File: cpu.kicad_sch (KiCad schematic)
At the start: 53 parts, among them IC12 DS2401+, IC13 ARM250, IC20 74HC138, IC27 74AC32, IC8 74HCT14, X100 40.0MHz, X4 72.0MHz, X5 25.175MHz

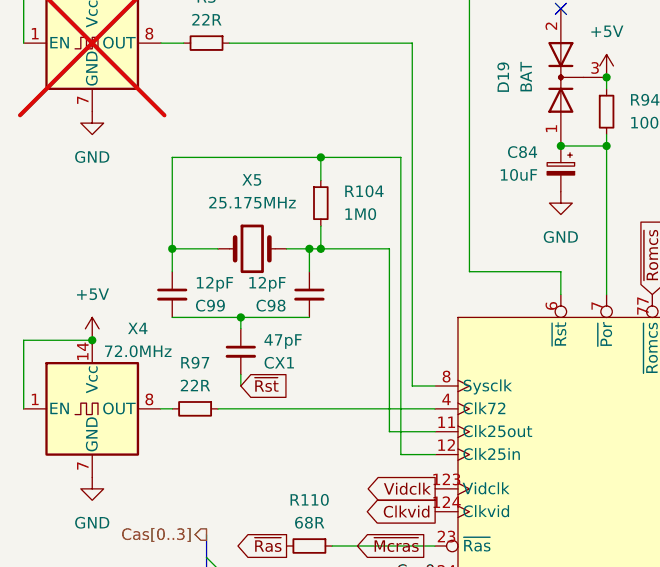
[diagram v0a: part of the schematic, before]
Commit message: fix CX1
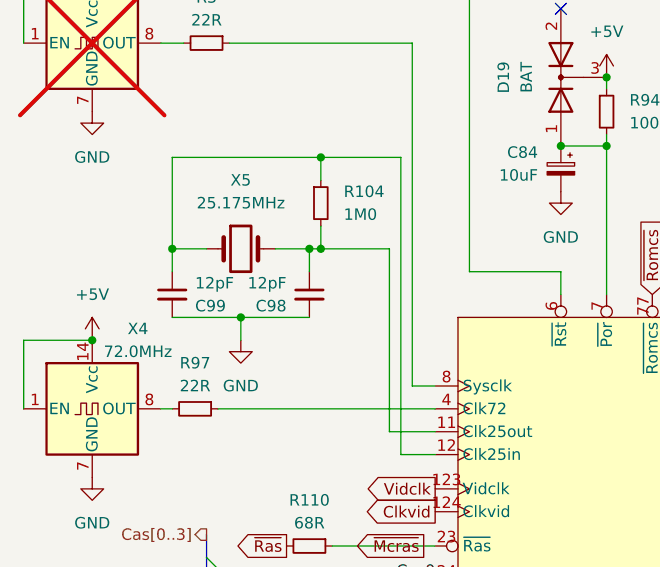
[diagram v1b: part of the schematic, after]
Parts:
- removed CX1: 47pF, Capacitor_THT:C_Axial_L5.1mm_D3.1mm_P12.50mm_Horizontal, symbol Device:C_Small
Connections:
- net GND: now also C98.2, C99.2
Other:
- moved on the sheet: X5
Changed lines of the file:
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@@
 	)
 	(junction
-		(at 71.12 88.9)
-		(diameter 0)
-		(color 0 0 0 0)
-	)
-	(junction
 		(at 187.96 86.36)
 		(diameter 0)
@@
 		(color 0 0 0 0)
 	)
+	(junction
+		(at 71.12 88.9)
+		(diameter 0)
+		(color 0 0 0 0)
+	)
 	(no_connect
 		(at 382.27 57.15)
@@
 	(wire
 		(pts
-			(xy 76.2 81.28) (xy 78.74 81.28)
+			(xy 74.93 81.28) (xy 78.74 81.28)
 		)
 		(stroke
@@
 	(wire
 		(pts
-			(xy 71.12 88.9) (xy 71.12 90.17)
-		)
-		(stroke
-			(width 0)
-			(type default)
-		)
-	)
-	(wire
-		(pts
 			(xy 68.58 137.16) (xy 73.66 137.16)
 		)
@@
 		)
 	)
-	(wire
-		(pts
-			(xy 71.12 96.52) (xy 71.12 95.25)
-		)
-		(stroke
-			(width 0)
-			(type default)
-		)
-	)
 	(bus
 		(pts
@@
 	(wire
 		(pts
-			(xy 71.12 88.9) (xy 78.74 88.9)
-		)
-		(stroke
-			(width 0)
-			(type default)
-		)
-	)
-	(wire
-		(pts
 			(xy 186.69 232.41) (xy 189.23 232.41)
 		)
@@
 	(wire
 		(pts
+			(xy 71.12 88.9) (xy 71.12 91.44)
+		)
+		(stroke
+			(width 0)
+			(type default)
+		)
+	)
+	(wire
+		(pts
 			(xy 193.04 86.36) (xy 195.58 86.36)
 		)
@@
 	(wire
 		(pts
+			(xy 71.12 88.9) (xy 78.74 88.9)
+		)
+		(stroke
+			(width 0)
+			(type default)
+		)
+	)
+	(wire
+		(pts
 			(xy 80.01 196.85) (xy 81.28 196.85)
 		)
@@
 	(wire
 		(pts
-			(xy 68.58 81.28) (xy 63.5 81.28)
+			(xy 67.31 81.28) (xy 63.5 81.28)
 		)
 		(stroke
@@
 		)
 	)
-	(global_label "~{Rst}"
-		(shape input)
-		(at 71.12 96.52 0)
-		(fields_autoplaced yes)
-		(effects
-			(font
-				(size 1.27 1.27)
-			)
-			(justify left)
-		)
-		(property "Intersheetrefs" "${INTERSHEET_REFS}"
-			(at 77.129 96.52 0)
-			(effects
-				(font
-					(size 1.27 1.27)
-				)
-				(justify left)
-				(hide yes)
-			)
-		)
-	)
 	(global_label "SndVSS"
 		(shape passive)
@@
 	(symbol
 		(lib_id "Device:Crystal")
-		(at 72.39 81.28 0)
+		(at 71.12 81.28 0)
 		(unit 1)
 		(exclude_from_sim no)
@@
 		(fields_autoplaced yes)
 		(property "Reference" "X5"
-			(at 72.39 73.66 0)
+			(at 71.12 73.66 0)
 			(effects
 				(font
@@
 		)
 		(property "Value" "25.175MHz"
-			(at 72.39 76.2 0)
+			(at 71.12 76.2 0)
 			(effects
 				(font
@@
 		)
 		(property "Footprint" "Crystal:Crystal_HC49-4H_Vertical"
-			(at 72.39 81.28 0)
+			(at 71.12 81.28 0)
 			(effects
 				(font
@@
 		)
 		(property "Datasheet" "~"
-			(at 72.39 81.28 0)
+			(at 71.12 81.28 0)
 			(effects
 				(font
@@
 		)
 		(property "Description" "Two pin crystal"
-			(at 72.39 81.28 0)
+			(at 71.12 81.28 0)
 			(effects
 				(font
@@
 	)
 	(symbol
-		(lib_id "Device:C_Small")
-		(at 71.12 92.71 0)
-		(mirror y)
-		(unit 1)
-		(exclude_from_sim no)
-		(in_bom yes)
-		(on_board yes)
-		(dnp no)
-		(property "Reference" "CX1"
-			(at 73.66 93.9865 0)
-			(effects
-				(font
-					(size 1.27 1.27)
-				)
-				(justify right)
-			)
-		)
-		(property "Value" "47pF"
-			(at 73.66 91.4465 0)
-			(effects
-				(font
-					(size 1.27 1.27)
-				)
-				(justify right)
-			)
-		)
-		(property "Footprint" "Capacitor_THT:C_Axial_L5.1mm_D3.1mm_P12.50mm_Horizontal"
-			(at 71.12 92.71 0)
-			(effects
-				(font
-					(size 1.27 1.27)
-				)
-				(hide yes)
-			)
-		)
-		(property "Datasheet" "~"
-			(at 71.12 92.71 0)
-			(effects
-				(font
-					(size 1.27 1.27)
-				)
-				(hide yes)
-			)
-		)
-		(property "Description" "Unpolarized capacitor, small symbol"
-			(at 71.12 92.71 0)
-			(effects
-				(font
-					(size 1.27 1.27)
-				)
-				(hide yes)
-			)
-		)
-		(pin "1"
-		)
-		(pin "2"
-		)
-		(instances
-			(project "Acorn-A3010"
-				(path "/999882f3-94f8-4a89-9093-27a47d0cb289/5f74aac3-9761-4bed-8486-119acb837e61"
-					(reference "CX1")
-					(unit 1)
-				)
-			)
-		)
-	)
-	(symbol
 		(lib_id "power:GND")
 		(at 54.61 106.68 0)
@@
 					(unit 1)
 				)
+			)
+		)
+	)
+	(symbol
+		(lib_id "power:GND")
+		(at 71.12 91.44 0)
+		(unit 1)
+		(exclude_from_sim no)
+		(in_bom yes)
+		(on_board yes)
+		(dnp no)
+		(fields_autoplaced yes)
+		(property "Reference" "#PWR063"
+			(at 71.12 97.79 0)
+			(effects
+				(font
+					(size 1.27 1.27)
+				)
+				(hide yes)
+			)
+		)
+		(property "Value" "GND"
+			(at 71.12 96.52 0)
+			(effects
+				(font
+					(size 1.27 1.27)
+				)
+			)
+		)
+		(property "Footprint" ""
+			(at 71.12 91.44 0)
+			(effects
+				(font
+					(size 1.27 1.27)
+				)
+				(hide yes)
+			)
+		)
+		(property "Datasheet" ""
+			(at 71.12 91.44 0)
+			(effects
+				(font
+					(size 1.27 1.27)
+				)
+				(hide yes)
+			)
+		)
+		(property "Description" "Power symbol creates a global label with name \"GND\" , ground"
+			(at 71.12 91.44 0)
+			(effects
+				(font
+					(size 1.27 1.27)
+				)
+				(hide yes)
+			)
+		)
+		(pin "1"
+		)
+		(instances
+			(project "Acorn-A3010"
+				(path "/999882f3-94f8-4a89-9093-27a47d0cb289/5f74aac3-9761-4bed-8486-119acb837e61"
+					(reference "#PWR063")
+					(unit 1)
+				)

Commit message: update design to correct errors found by IanJ
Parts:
- removed D19: BAT, Package_TO_SOT_SMD:SOT-23-3, symbol Device:D_Dual_CommonCathode_AAK
- removed TP1: C1, TestPoint:TestPoint_Pad_D1.0mm, symbol Connector:TestPoint
- removed TP6: C0, TestPoint:TestPoint_Pad_D1.0mm, symbol Connector:TestPoint
- added D19: BAS16, PCM_Package_TO_SOT_SMD_AKL:SOT-23, symbol PCM_Diode_AKL:BAS16
- R608: renamed from R4; value 4K7 -> 33R; LCSC C2907326 -> (none); LCSC Part C2907326 -> (none)
- RP11: value 100Kx8 -> 68Rx8; LCSC C1738931 -> (none); LCSC Part C1738931 -> (none)
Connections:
- net +5V: now also D19.3 (K)
- net at C84.1, IC13.7 (~{Por}), R94.2: now also D19.1 (A)
- no-connect marks 11 -> 10

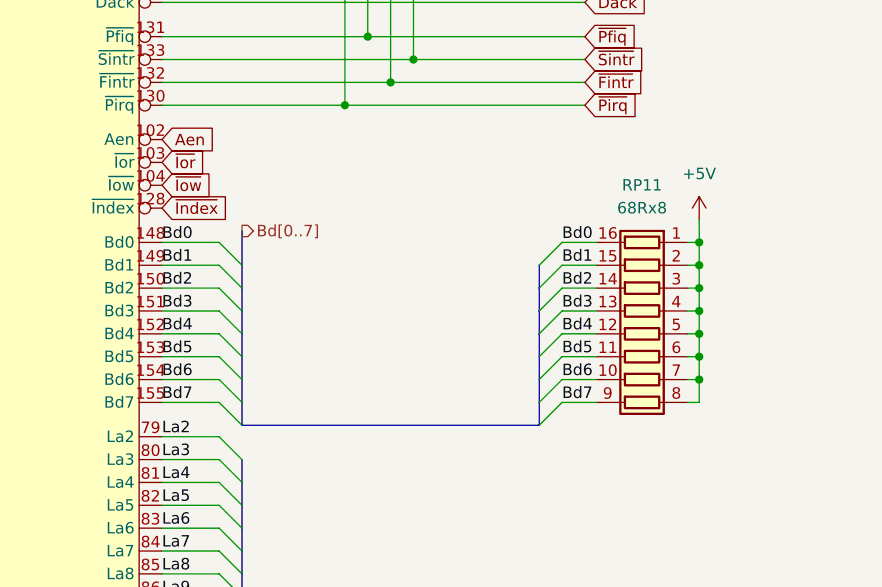
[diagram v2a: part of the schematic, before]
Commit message: move RP11 inline instead of pullup
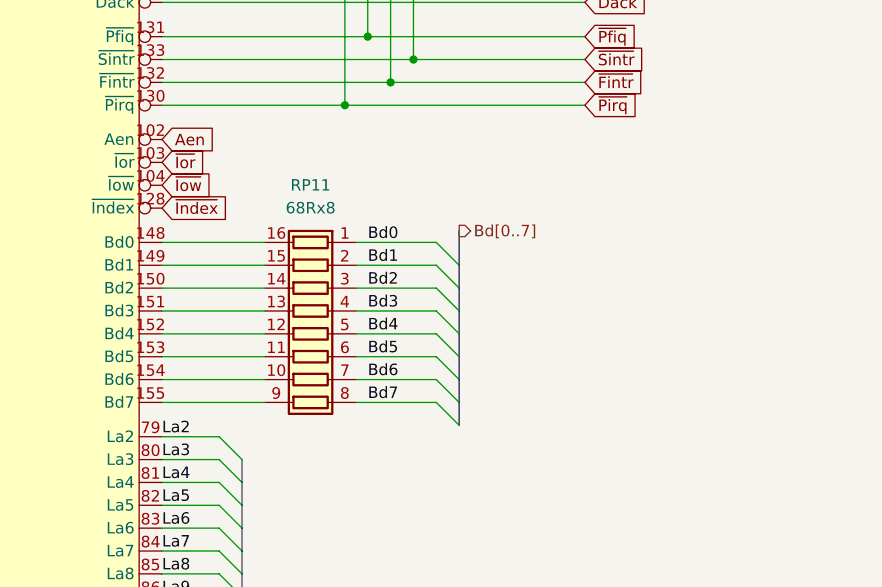
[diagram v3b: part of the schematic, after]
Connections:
- net +5V: no longer RP11.1 (R1.1), RP11.2 (R2.1), RP11.3 (R3.1), RP11.4 (R4.1), RP11.5 (R5.1), RP11.6 (R6.1), RP11.7 (R7.1), RP11.8 (R8.1)
- net Bd0: now also RP11.1 (R1.1); no longer IC13.148 (Bd0), RP11.16 (R1.2)
- net Bd1: now also RP11.2 (R2.1); no longer IC13.149 (Bd1), RP11.15 (R2.2)
- net Bd2: now also RP11.3 (R3.1); no longer IC13.150 (Bd2), RP11.14 (R3.2)
- net Bd3: now also RP11.4 (R4.1); no longer IC13.151 (Bd3), RP11.13 (R4.2)
- net Bd4: now also RP11.5 (R5.1); no longer IC13.152 (Bd4), RP11.12 (R5.2)
- net Bd5: now also RP11.6 (R6.1); no longer IC13.153 (Bd5), RP11.11 (R6.2)
- net Bd6: now also RP11.7 (R7.1); no longer IC13.154 (Bd6), RP11.10 (R7.2)
- net Bd7: now also RP11.8 (R8.1); no longer IC13.155 (Bd7), RP11.9 (R8.2)
- new net: IC13.154 (Bd6), RP11.10 (R7.2)
- new net: IC13.153 (Bd5), RP11.11 (R6.2)
- new net: IC13.152 (Bd4), RP11.12 (R5.2)
- new net: IC13.151 (Bd3), RP11.13 (R4.2)
- new net: IC13.150 (Bd2), RP11.14 (R3.2)
- new net: IC13.149 (Bd1), RP11.15 (R2.2)
- new net: IC13.148 (Bd0), RP11.16 (R1.2)
- new net: IC13.155 (Bd7), RP11.9 (R8.2)
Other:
- moved on the sheet: RP11

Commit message: fix missing ide signals
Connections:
- net ~{I13}: now reaches IC13.143 (~{I13}), R91.2, TP35.1
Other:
- moved on the sheet: TP35
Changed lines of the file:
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@@
 	(wire
 		(pts
-			(xy 220.98 105.41) (xy 220.98 109.22)
+			(xy 220.98 93.98) (xy 220.98 109.22)
 		)
 		(stroke
@@
 		)
 	)
+	(global_label "~{I13}"
+		(shape input)
+		(at 220.98 96.52 0)
+		(fields_autoplaced yes)
+		(effects
+			(font
+				(size 1.27 1.27)
+			)
+			(justify left)
+		)
+		(property "Intersheetrefs" "${INTERSHEET_REFS}"
+			(at 226.989 96.52 0)
+			(effects
+				(font
+					(size 1.27 1.27)
+				)
+				(justify left)
+				(hide yes)
+			)
+		)
+	)
 	(global_label "Clkvid"
 		(shape output)
@@
 	(symbol
 		(lib_id "Connector:TestPoint")
-		(at 220.98 105.41 0)
+		(at 220.98 93.98 0)
 		(unit 1)
 		(exclude_from_sim no)
@@
 		(fields_autoplaced yes)
 		(property "Reference" "TP35"
-			(at 223.52 100.8379 0)
+			(at 223.52 89.4079 0)
 			(effects
 				(font
@@
 		)
 		(property "Value" "I13"
-			(at 223.52 103.3779 0)
+			(at 223.52 91.9479 0)
 			(effects
 				(font
@@
 		)
 		(property "Footprint" "TestPoint:TestPoint_Pad_D1.0mm"
-			(at 226.06 105.41 0)
+			(at 226.06 93.98 0)
 			(effects
 				(font
@@
 		)
 		(property "Datasheet" "~"
-			(at 226.06 105.41 0)
+			(at 226.06 93.98 0)
 			(effects
 				(font
@@
 		)
 		(property "Description" "test point"
-			(at 220.98 105.41 0)
+			(at 220.98 93.98 0)
 			(effects
 				(font
